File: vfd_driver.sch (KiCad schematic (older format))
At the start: 32 parts, among them J1 Input, J2 futaba_7_lt_44z, J3 High Volt, J4 FIL_n, J5 FIL_p, Q3 BC817, Q4 BC807, Q5 BC817, Q6 BC807, U2 74HC595, U3 74HC595, U4 74HC595, U5 TBD62783A, U6 TBD62783A, U7 TBD62783A

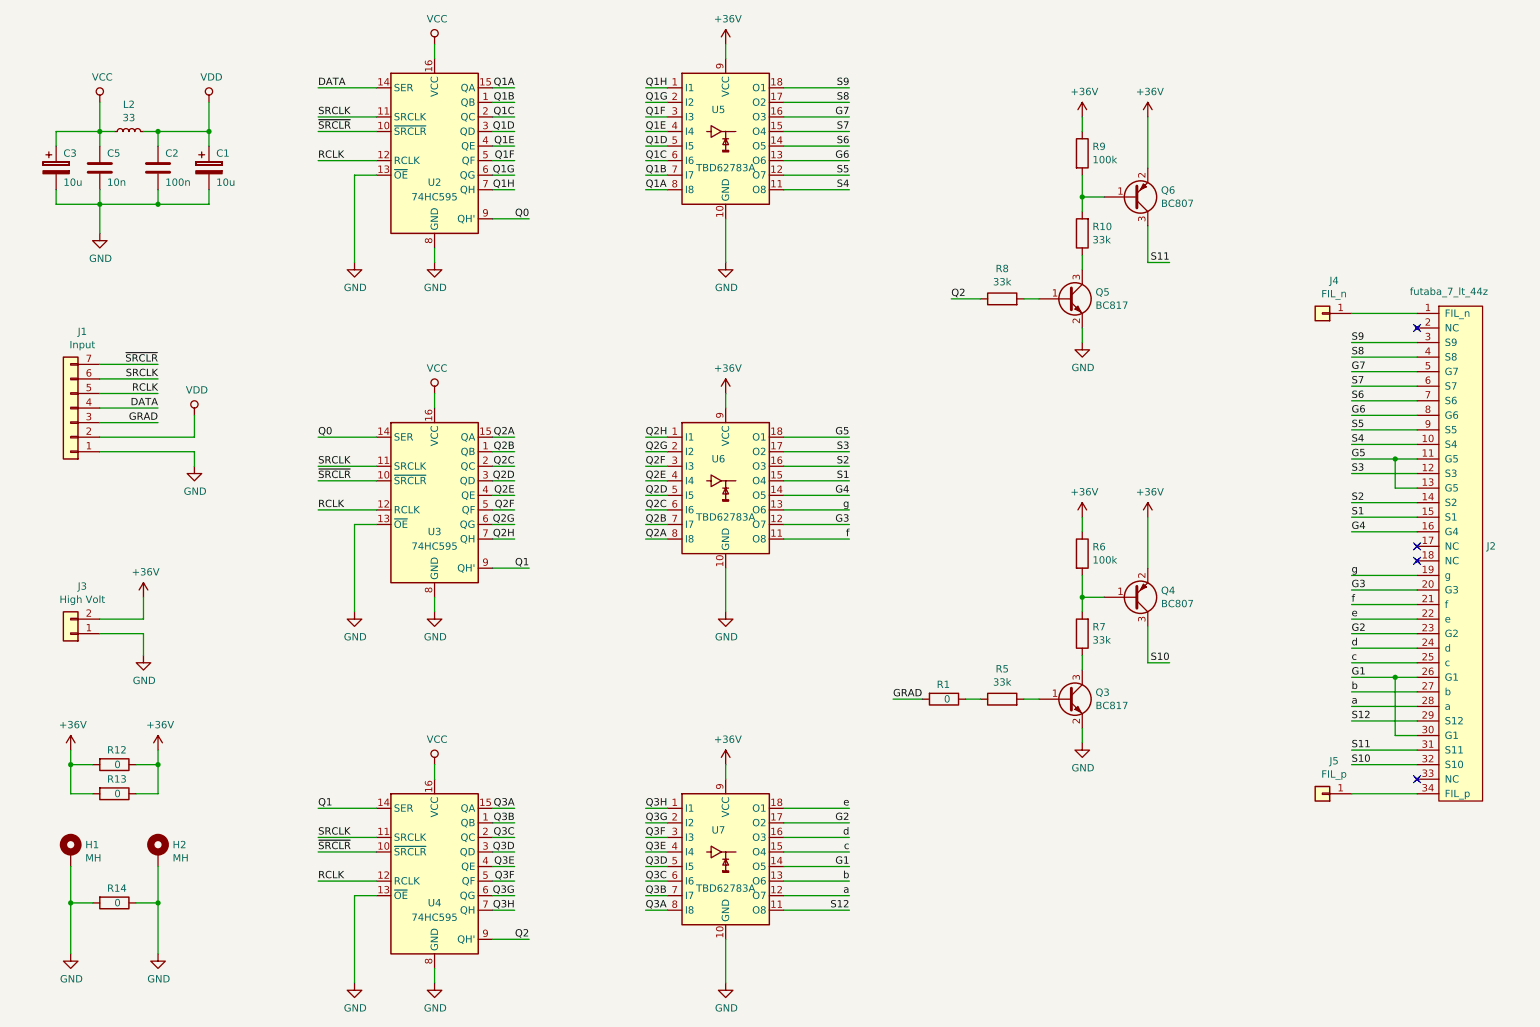
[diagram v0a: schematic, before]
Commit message: Add a 4th shift register and suppress the grad-pin input
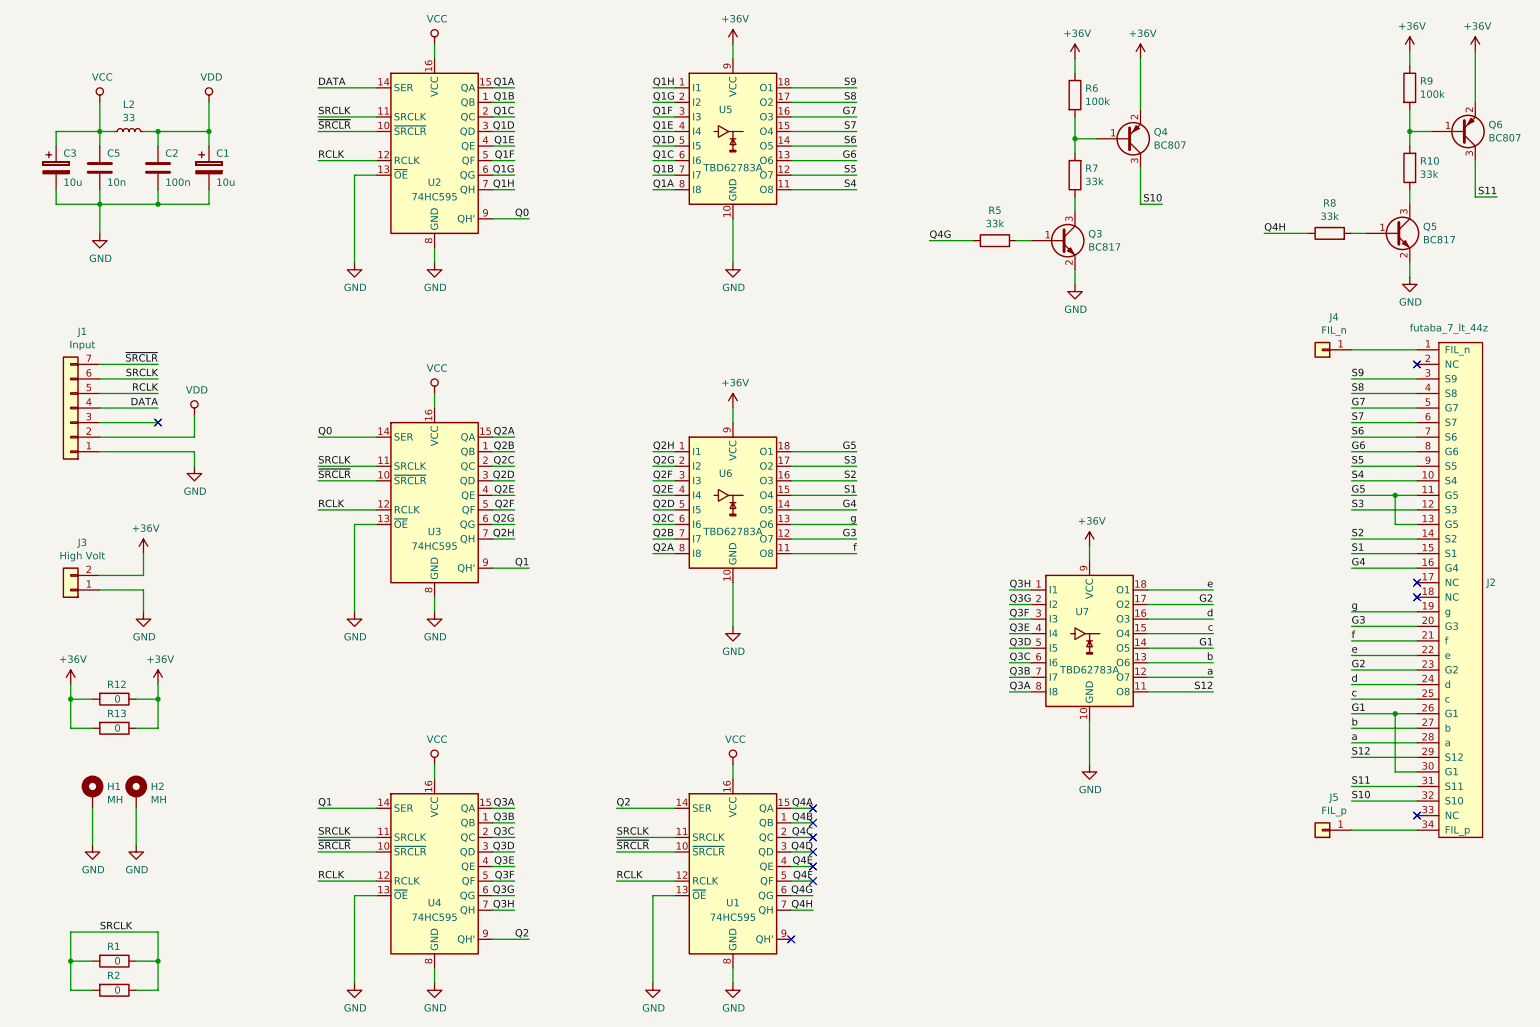
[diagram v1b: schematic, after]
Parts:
- removed R14: 0, Resistor_SMD:R_1206_3216Metric, symbol Device:R
- added R2: 0, Resistor_SMD:R_1206_3216Metric, symbol Device:R
- added U1: 74HC595, Package_SO:SOIC-16_3.9x9.9mm_P1.27mm, symbol 74xx:74HC595
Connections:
- net GND: now also U1.13 (~OE), U1.8 (GND)
- net Q2: now also U1.14 (SER); no longer R8.1
- net RCLK: now also U1.12 (RCLK)
- net SRCLK: now also R1.1, R1.2, R2.1, R2.2, U1.11 (SRCLK)
- net VCC: now also U1.16 (VCC)
- net ~SRCLR: now also U1.10 (~SRCLR)
- net Q4G: now reaches R5.1
- net Q4G: now also U1.6 (QG); no longer R1.1
- net GRAD: no longer names the net of J1.3 (Pin_3)
- net GRAD: no longer R1.2
- new net Q4A: U1.15 (QA)
- new net Q4B: U1.1 (QB)
- new net Q4C: U1.2 (QC)
- new net Q4D: U1.3 (QD)
- new net Q4E: U1.4 (QE)
- new net Q4F: U1.5 (QF)
- new net Q4H: R8.1, U1.7 (QH)
- no-connect marks 4 -> 12
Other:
- moved on the sheet: H1, H2, J2, J3, J4, J5, Q3, Q4, Q5, Q6, R10, R12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

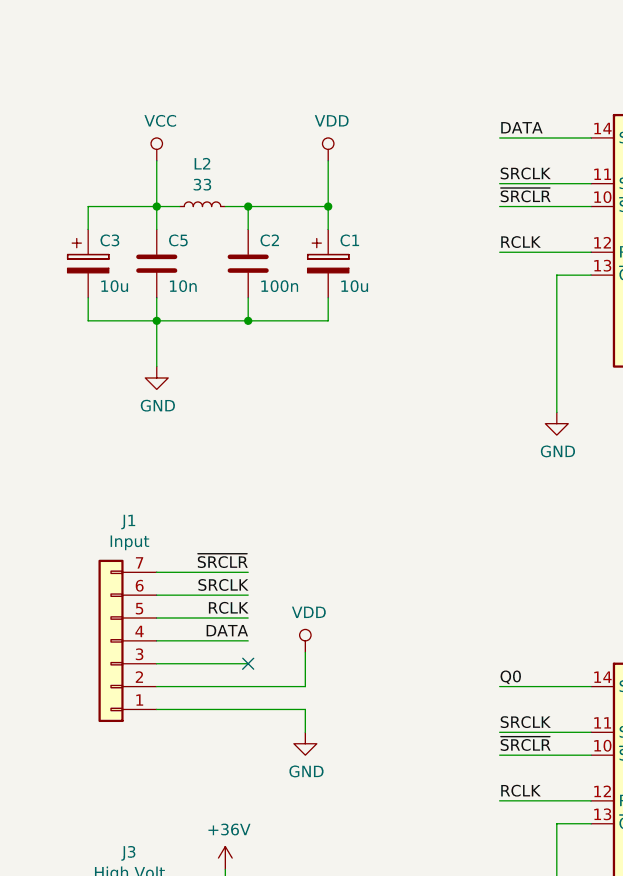
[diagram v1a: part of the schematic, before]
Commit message: add a protecting diode to the power input.
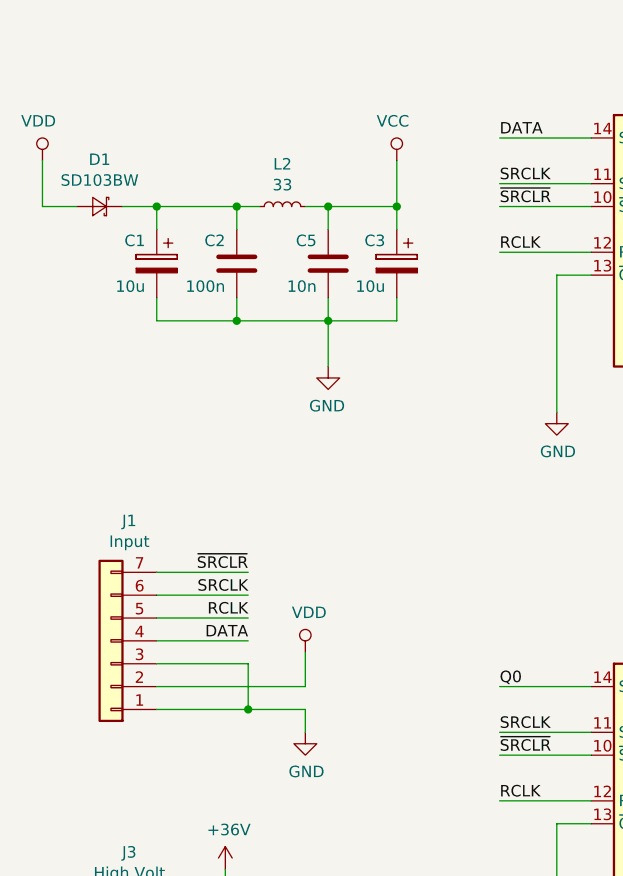
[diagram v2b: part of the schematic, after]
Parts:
- added D1: SD103BW, Diode_SMD:D_SOD-123, symbol Device:D_Schottky_Small
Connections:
- net GND: now also J1.3 (Pin_3)
- net VDD: now also D1.2 (A); no longer C1.1, C2.1, L2.2
- new net: C1.1, C2.1, D1.1 (K), L2.2
- no-connect marks 12 -> 11
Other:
- moved on the sheet: C1, C2, C3, C5, L2
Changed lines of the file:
@@
 L power:GND #PWR02
 U 1 1 5C03E104
-P 1300 2200
-F 0 "#PWR02" H 1300 1950 50  0001 C CNN
-F 1 "GND" H 1305 2027 50  0000 C CNN
-F 2 "" H 1300 2200 50  0001 C CNN
-F 3 "" H 1300 2200 50  0001 C CNN
-	1    1300 2200
-	1    0    0    -1
+P 2050 2200
+F 0 "#PWR02" H 2050 1950 50  0001 C CNN
+F 1 "GND" H 2055 2027 50  0000 C CNN
+F 2 "" H 2050 2200 50  0001 C CNN
+F 3 "" H 2050 2200 50  0001 C CNN
+	1    2050 2200
+	-1   0    0    -1
 $EndComp
 $Comp
 L power:VCC #PWR01
 U 1 1 5C047331
-P 1300 1300
-F 0 "#PWR01" H 1300 1150 50  0001 C CNN
-F 1 "VCC" H 1317 1473 50  0000 C CNN
-F 2 "" H 1300 1300 50  0001 C CNN
-F 3 "" H 1300 1300 50  0001 C CNN
-	1    1300 1300
-	1    0    0    -1
+P 2350 1300
+F 0 "#PWR01" H 2350 1150 50  0001 C CNN
+F 1 "VCC" H 2367 1473 50  0000 C CNN
+F 2 "" H 2350 1300 50  0001 C CNN
+F 3 "" H 2350 1300 50  0001 C CNN
+	1    2350 1300
+	-1   0    0    -1
 $EndComp
 $Comp
 L Device:C C2
 U 1 1 5C048B36
-P 1700 1750
-F 0 "C2" H 1750 1850 50  0000 L CNN
-F 1 "100n" H 1750 1650 50  0000 L CNN
-F 2 "Capacitor_SMD:C_0805_2012Metric_Pad1.15x1.40mm_HandSolder" H 1738 1600 50  0001 C CNN
-F 3 "~" H 1700 1750 50  0001 C CNN
-	1    1700 1750
-	1    0    0    -1
+P 1650 1750
+F 0 "C2" H 1700 1850 50  0000 L CNN
+F 1 "100n" H 1700 1650 50  0000 L CNN
+F 2 "Capacitor_SMD:C_0805_2012Metric_Pad1.15x1.40mm_HandSolder" H 1688 1600 50  0001 C CNN
+F 3 "~" H 1650 1750 50  0001 C CNN
+	1    1650 1750
+	-1   0    0    -1
 $EndComp
 $Comp
 L Device:CP C1
 U 1 1 5C048CF5
-P 2050 1750
-F 0 "C1" H 2100 1850 50  0000 L CNN
-F 1 "10u" H 2100 1650 50  0000 L CNN
-F 2 "Capacitor_THT:CP_Radial_D8.0mm_P3.80mm" H 2088 1600 50  0001 C CNN
-F 3 "~" H 2050 1750 50  0001 C CNN
-	1    2050 1750
-	1    0    0    -1
-$EndComp
-Wire Wire Line
-	2050 2000 2050 1900
-Wire Wire Line
-	2050 1600 2050 1500
+P 1300 1750
+F 0 "C1" H 1350 1850 50  0000 L CNN
+F 1 "10u" H 1350 1650 50  0000 L CNN
+F 2 "Capacitor_THT:CP_Radial_D8.0mm_P3.80mm" H 1338 1600 50  0001 C CNN
+F 3 "~" H 1300 1750 50  0001 C CNN
+	1    1300 1750
+	-1   0    0    -1
+$EndComp
+Wire Wire Line
+	1300 2000 1300 1900
+Wire Wire Line
+	1300 1600 1300 1500
 $Comp
 L 74xx:74HC595 U2
@@
 L Device:L_Small L2
 U 1 1 5C691AE0
-P 1500 1500
-F 0 "L2" V 1685 1500 50  0000 C CNN
-F 1 "33" V 1594 1500 50  0000 C CNN
-F 2 "Inductor_SMD:L_1206_3216Metric_Pad1.42x1.75mm_HandSolder" H 1500 1500 50  0001 C CNN
-F 3 "~" H 1500 1500 50  0001 C CNN
-	1    1500 1500
-	0    -1   -1   0
-$EndComp
-Connection ~ 2050 1500
+P 1850 1500
+F 0 "L2" V 2035 1500 50  0000 C CNN
+F 1 "33" V 1944 1500 50  0000 C CNN
+F 2 "Inductor_SMD:L_1206_3216Metric_Pad1.42x1.75mm_HandSolder" H 1850 1500 50  0001 C CNN
+F 3 "~" H 1850 1500 50  0001 C CNN
+	1    1850 1500
+	0    1    -1   0
+$EndComp
 $Comp
 L Device:C C5
 U 1 1 5C70EF22
-P 1300 1750
-F 0 "C5" H 1350 1850 50  0000 L CNN
-F 1 "10n" H 1350 1650 50  0000 L CNN
-F 2 "Capacitor_SMD:C_0805_2012Metric_Pad1.15x1.40mm_HandSolder" H 1338 1600 50  0001 C CNN
-F 3 "~" H 1300 1750 50  0001 C CNN
-	1    1300 1750
-	1    0    0    -1
-$EndComp
-Wire Wire Line
-	1300 1300 1300 1500
-Wire Wire Line
-	1300 1500 1400 1500
-Connection ~ 1300 1500
-Wire Wire Line
-	1300 1500 1300 1600
-Wire Wire Line
-	1700 1500 1700 1600
-Wire Wire Line
-	1700 1900 1700 2000
-Wire Wire Line
-	2050 1300 2050 1500
-Wire Wire Line
-	1300 1900 1300 2000
-Connection ~ 1700 1500
-Connection ~ 1700 2000
-Connection ~ 1300 2000
-Wire Wire Line
-	1300 2000 1300 2200
-Wire Wire Line
-	1700 1500 2050 1500
-Wire Wire Line
-	1700 2000 2050 2000
-Wire Wire Line
-	1600 1500 1700 1500
-Wire Wire Line
-	1300 2000 1700 2000
+P 2050 1750
+F 0 "C5" H 2100 1850 50  0000 L CNN
+F 1 "10n" H 2100 1650 50  0000 L CNN
+F 2 "Capacitor_SMD:C_0805_2012Metric_Pad1.15x1.40mm_HandSolder" H 2088 1600 50  0001 C CNN
+F 3 "~" H 2050 1750 50  0001 C CNN
+	1    2050 1750
+	-1   0    0    -1
+$EndComp
+Wire Wire Line
+	2350 1300 2350 1500
+Wire Wire Line
+	2050 1500 1950 1500
+Connection ~ 2050 1500
+Wire Wire Line
+	2050 1500 2050 1600
+Wire Wire Line
+	1650 1500 1650 1600
+Wire Wire Line
+	1650 1900 1650 2000
+Wire Wire Line
+	800  1300 800  1500
+Wire Wire Line
+	2050 1900 2050 2000
+Connection ~ 1650 1500
+Connection ~ 1650 2000
+Connection ~ 2050 2000
+Wire Wire Line
+	2050 2000 2050 2200
+Wire Wire Line
+	1650 1500 1300 1500
+Wire Wire Line
+	1650 2000 1300 2000
+Wire Wire Line
+	1750 1500 1650 1500
+Wire Wire Line
+	2050 2000 1650 2000
 $Comp
 L Device:CP C3
 U 1 1 5CBED78A
-P 1000 1750
-F 0 "C3" H 1050 1850 50  0000 L CNN
-F 1 "10u" H 1050 1650 50  0000 L CNN
-F 2 "Capacitor_THT:CP_Radial_D8.0mm_P3.80mm" H 1038 1600 50  0001 C CNN
-F 3 "~" H 1000 1750 50  0001 C CNN
-	1    1000 1750
-	1    0    0    -1
-$EndComp
-Wire Wire Line
-	1300 1500 1000 1500
-Wire Wire Line
-	1000 1500 1000 1600
-Wire Wire Line
-	1000 1900 1000 2000
-Wire Wire Line
-	1000 2000 1300 2000
+P 2350 1750
+F 0 "C3" H 2400 1850 50  0000 L CNN
+F 1 "10u" H 2400 1650 50  0000 L CNN
+F 2 "Capacitor_THT:CP_Radial_D8.0mm_P3.80mm" H 2388 1600 50  0001 C CNN
+F 3 "~" H 2350 1750 50  0001 C CNN
+	1    2350 1750
+	-1   0    0    -1
+$EndComp
+Wire Wire Line
+	2050 1500 2350 1500
+Wire Wire Line
+	2350 1500 2350 1600
+Wire Wire Line
+	2350 1900 2350 2000
+Wire Wire Line
+	2350 2000 2050 2000
 $Comp
 L Connector_Generic:Conn_01x01 J4
@@
 L power:VDD #PWR0103
 U 1 1 5C920C13
-P 2050 1300
-F 0 "#PWR0103" H 2050 1150 50  0001 C CNN
-F 1 "VDD" H 2067 1473 50  0000 C CNN
-F 2 "" H 2050 1300 50  0001 C CNN
-F 3 "" H 2050 1300 50  0001 C CNN
-	1    2050 1300
-	1    0    0    -1
+P 800 1300
+F 0 "#PWR0103" H 800 1150 50  0001 C CNN
+F 1 "VDD" H 817 1473 50  0000 C CNN
+F 2 "" H 800 1300 50  0001 C CNN
+F 3 "" H 800 1300 50  0001 C CNN
+	1    800  1300
+	-1   0    0    -1
 $EndComp
 $Comp
@@
 	1300 3600 1950 3600
 Wire Wire Line
-	1300 3700 1950 3700
+	1300 3700 1700 3700
 Wire Wire Line
 	4000 2100 4250 2100
@@
 NoConn ~ 6200 6550
 NoConn ~ 6200 6650
-NoConn ~ 1700 3500
 Wire Wire Line
 	7000 2250 7300 2250
@@
 Wire Wire Line
 	1100 7000 1100 7200
+Wire Wire Line
+	1700 3500 1700 3700
+Connection ~ 1700 3700
+Wire Wire Line
+	1700 3700 1950 3700
+$Comp
+L Device:D_Schottky_Small D1
+U 1 1 5CC07EAB
+P 1050 1500
+F 0 "D1" H 1050 1705 50  0000 C CNN
+F 1 "SD103BW" H 1050 1614 50  0000 C CNN
+F 2 "Diode_SMD:D_SOD-123" V 1050 1500 50  0001 C CNN
+F 3 "~" V 1050 1500 50  0001 C CNN
+	1    1050 1500
+	-1   0    0    -1
+$EndComp
+Connection ~ 2350 1500
+Wire Wire Line
+	800  1500 950  1500
+Wire Wire Line
+	1150 1500 1300 1500
+Connection ~ 1300 1500
 $EndSCHEMATC

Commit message: before adding lt1073
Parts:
- removed C1: 10u, Capacitor_THT:CP_Radial_D8.0mm_P3.80mm, symbol Device:CP
- removed C2: 100n, Capacitor_SMD:C_0805_2012Metric_Pad1.15x1.40mm_HandSolder, symbol Device:C
- removed D1: SD103BW, Diode_SMD:D_SOD-123, symbol Device:D_Schottky_Small
- removed J1: Input, Connector_PinSocket_2.54mm:PinSocket_1x07_P2.54mm_Vertical, symbol Connector_Generic:Conn_01x07
- removed J2: futaba_7_lt_44z, Connector_PinSocket_2.54mm:PinSocket_1x34_P2.54mm_Vertical, symbol vfd_driver-rescue:futaba_7_lt_44z-custom-vfd_driver-rescue
- removed J4: FIL_n, Connector_Pin:Pin_D1.4mm_L8.5mm_W2.8mm_FlatFork, symbol Connector_Generic:Conn_01x01
- removed J5: FIL_p, Connector_Pin:Pin_D1.4mm_L8.5mm_W2.8mm_FlatFork, symbol Connector_Generic:Conn_01x01
- removed L2: 33, Inductor_SMD:L_1206_3216Metric_Pad1.42x1.75mm_HandSolder, symbol Device:L_Small
- removed Q3, Q5: BC817, Package_TO_SOT_SMD:SOT-23, symbol Transistor_BJT:BC817
- removed Q4, Q6: BC807, Package_TO_SOT_SMD:SOT-23, symbol Transistor_BJT:BC807
- removed R10, R5, R7, R8: 33k, Resistor_SMD:R_0805_2012Metric_Pad1.15x1.40mm_HandSolder, symbol Device:R
- removed R12, R13: 0, Resistor_SMD:R_1206_3216Metric, symbol Device:R
- removed R6, R9: 100k, Resistor_SMD:R_0805_2012Metric_Pad1.15x1.40mm_HandSolder, symbol Device:R
- removed U1, U2, U3, U4: 74HC595, Package_SO:SOIC-16_3.9x9.9mm_P1.27mm, symbol 74xx:74HC595
- removed U5, U6, U7: TBD62783A, Package_SO:SOP-18_7.0x12.5mm_P1.27mm, symbol Transistor_Array:TBD62783A
- added C4: 10u/63v, Capacitor_THT:CP_Radial_D8.0mm_P5.00mm, symbol Device:CP
- added C6: 4n7, Capacitor_SMD:C_0805_2012Metric_Pad1.15x1.40mm_HandSolder, symbol Device:C
- added C7: 1u, Capacitor_THT:C_Rect_L7.0mm_W2.0mm_P5.00mm, symbol Device:C
- added C8: 100n, Capacitor_THT:C_Rect_L7.0mm_W2.0mm_P5.00mm, symbol Device:C
- added C9: 10n, Capacitor_SMD:C_0805_2012Metric_Pad1.15x1.40mm_HandSolder, symbol Device:C
- added D1: SD_103BW, Diode_SMD:D_SOD-123, symbol Device:D_Schottky
- added D2: SS14, Diode_SMD:D_SMA_Handsoldering, symbol Device:D_Schottky
- added D3: 1N4148, Diode_SMD:D_MiniMELF, symbol Device:D_Small
- added J1: Input, Connector_PinHeader_2.54mm:PinHeader_1x02_P2.54mm_Vertical, symbol Connector_Generic:Conn_01x02
- added J2: FIL, Connector_PinHeader_2.54mm:PinHeader_1x02_P2.54mm_Vertical, symbol Connector_Generic:Conn_01x02
- added L1: 330, Choke_SMD:Choke_CD75, symbol Device:L
- added Q1: IRLZ34, Package_TO_SOT_THT:TO-220-3_Vertical, symbol Device:Q_NMOS_GDS
- added R14: 0, Resistor_SMD:R_1206_3216Metric, symbol Device:R
- added R15, R3: 22k, Resistor_SMD:R_0805_2012Metric_Pad1.15x1.40mm_HandSolder, symbol Device:R_Small
- added R16, R17: 18, Resistor_SMD:R_1206_3216Metric_Pad1.42x1.75mm_HandSolder, symbol Device:R
- added R18: 4k7, Resistor_SMD:R_0805_2012Metric_Pad1.15x1.40mm_HandSolder, symbol Device:R_Small
- added R4: 10k, Resistor_SMD:R_0805_2012Metric_Pad1.15x1.40mm_HandSolder, symbol Device:R_Small
- added R5: 1k, Resistor_SMD:R_0805_2012Metric_Pad1.15x1.40mm_HandSolder, symbol Device:R_Small
- added U1: LM4871, Package_SO:SOIC-8_3.9x4.9mm_P1.27mm, symbol vfd_driver-rescue:LM4871-LM4871
- added U8: LM555, Package_DIP:DIP-8_W7.62mm_Socket_LongPads, symbol Timer:LM555
- C5: value 10n -> 100n
- J3: value High Volt -> HV
- R1: value 0 -> 1k; footprint Resistor_SMD:R_1206_3216Metric -> Resistor_SMD:R_0805_2012Metric_Pad1.15x1.40mm_HandSolder
- R2: value 0 -> 100k; footprint Resistor_SMD:R_1206_3216Metric -> Resistor_SMD:R_0805_2012Metric_Pad1.15x1.40mm_HandSolder
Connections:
- net +36V: now also J3.1 (Pin_1), C4.1, D2.1 (K); no longer J3.2 (Pin_2)
- net GND: now also J3.2 (Pin_2), R2.2, C4.2, C6.2, C7.2, C8.2, C9.2, D1.2 (A), J1.1 (Pin_1), Q1.3 (S), U1.1 (SHUTDWN), U1.7 (GND), U8.1 (GND); no longer J3.1 (Pin_1)
- net SRCLK: no longer names the net of R1.1, R2.1
- net SRCLK: now also Q1.1 (G); no longer R1.2, R2.2
- net VCC renamed +5V
- net +5V: now also J1.2 (Pin_2), L1.1, R14.1, R14.2, R5.1, U1.6 (VDD), U8.4 (R), U8.8 (VCC)
- new net: D1.1 (K), D2.2 (A), L1.2, Q1.2 (D)
- new net: D3.2 (A), R18.2, R5.2, U8.7 (DIS)
- new net: C8.1, D3.1 (K), R18.1, U8.2 (TR), U8.6 (THR)
- new net: C9.1, U8.5 (CV)
- new net: C7.1, R4.1, U1.2 (BYPASS)
- new net: R15.2, R4.2, U1.3 (IN+)
- new net: C6.1, R3.1, U1.4 (IN-)
- new net: R15.1, R16.1, R3.2, U1.5 (V01)
- new net: R17.1, U1.8 (V02)
- new net FIL_n: J2.1 (Pin_1), R16.2
- new net FIL_p: J2.2 (Pin_2), R17.2
- new net HV: R1.2, U8.3 (Q)
- no-connect marks 11 -> 0
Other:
- note added: "10K"
- note added: "470"
- moved on the sheet: C3, C5, H1, H2
